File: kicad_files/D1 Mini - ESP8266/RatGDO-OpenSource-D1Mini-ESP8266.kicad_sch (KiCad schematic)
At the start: 9 parts, among them J1 Screw_Terminal_01x03, J2 Screw_Terminal_01x03, J3 Screw_Terminal_01x03, Q1 2N7002, Q2 AO3400A, U1 WeMos_D1_mini

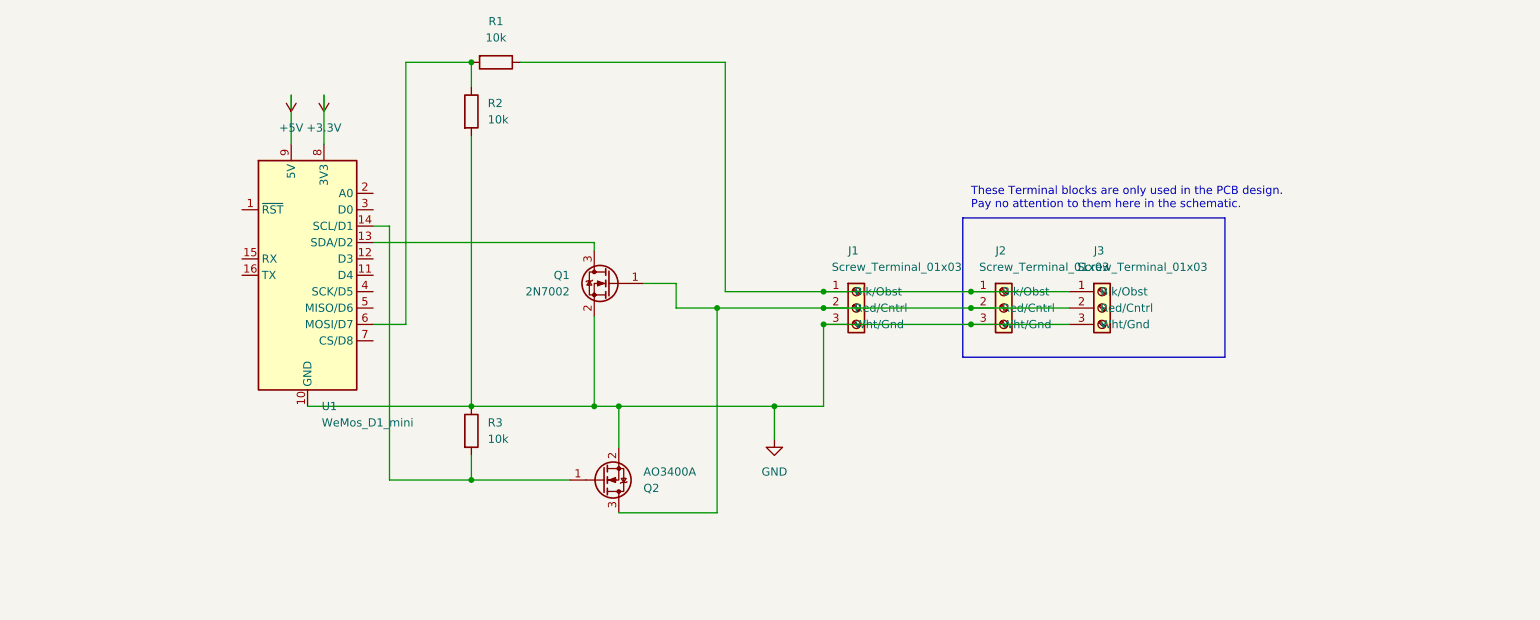
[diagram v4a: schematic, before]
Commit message: Update ESP8266 schematics and PCB
Added 1K R4 on gate of Q2.
Added 10K R5/R6 on gate of Q1.
Re-laid out PCB, all single sided and smaller.
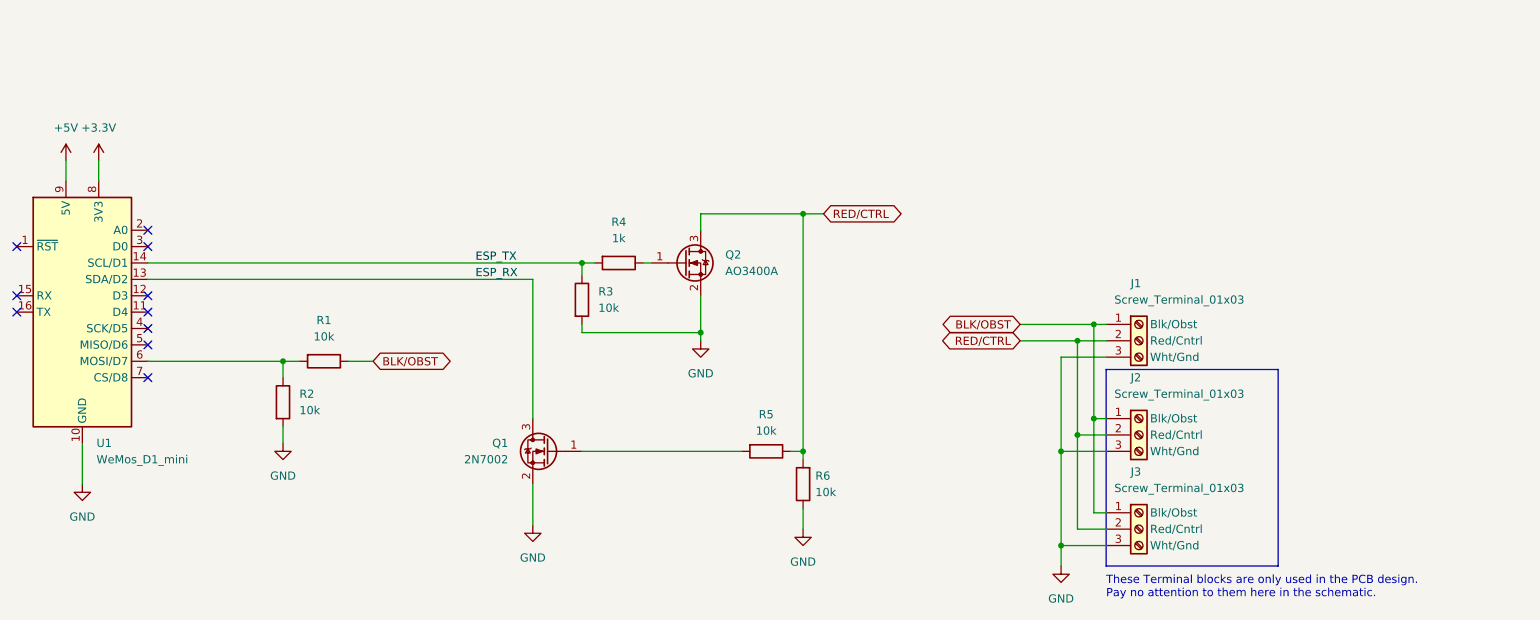
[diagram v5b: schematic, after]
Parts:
- added R4: 1k, Resistor_SMD:R_0805_2012Metric_Pad1.20x1.40mm_HandSolder, symbol Device:R
- added R5, R6: 10k, Resistor_SMD:R_0805_2012Metric_Pad1.20x1.40mm_HandSolder, symbol Device:R
- J3: footprint Connector_PinSocket_2.54mm:PinSocket_1x03_P2.54mm_Vertical -> Connector_PinHeader_2.54mm:PinHeader_1x03_P2.54mm_Vertical
- Q1, Q2: footprint Package_TO_SOT_SMD:SOT-23 -> Package_TO_SOT_SMD:SOT-23_Handsoldering
- R1, R2, R3: footprint Resistor_SMD:R_0805_2012Metric -> Resistor_SMD:R_0805_2012Metric_Pad1.20x1.40mm_HandSolder
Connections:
- net GND: now also R3.2, R6.1; no longer R3.1
- net ESP_RX: now reaches Q1.3 (D), U1.13 (SDA/D2)
- net BLK/OBST: now reaches J1.1 (Blk/Obst), J2.1 (Blk/Obst), J3.1 (Blk/Obst), R1.1
- net RED/CTRL: now reaches J1.2 (Red/Cntrl), J2.2 (Red/Cntrl), J3.2 (Red/Cntrl), Q2.3 (D)
- net RED/CTRL: now also R5.1, R6.2; no longer Q1.1 (G)
- new net: Q1.1 (G), R5.2
- new net: Q2.1 (G), R4.1
- new net ESP_TX: R3.1, R4.2, U1.14 (SCL/D1)
- no-connect marks 0 -> 10
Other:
- title: (none) -> RatGDO OpenSource D1Mini-ESP8266
- moved on the sheet: J1, J2, J3, Q1, Q2, R1, R2, R3, U1
